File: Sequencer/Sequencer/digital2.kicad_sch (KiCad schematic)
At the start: 4 parts, among them SW5 SW_Rotary12, SW6 SW_Push_DPDT, SW7 SW_Rotary4, U5 4514

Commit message: minor progress on sequencer
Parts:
- added C5 (x3): 1nF, Capacitor_THT:C_Disc_D3.0mm_W1.6mm_P2.50mm, symbol Device:C
- added D11 (x3): 1N914, Diode_THT:D_DO-35_SOD27_P7.62mm_Horizontal, symbol Diode:1N914
- added R12 (x2): 100K, Resistor_THT:R_Axial_DIN0207_L6.3mm_D2.5mm_P7.62mm_Horizontal, symbol Device:R
- added R12 (x2): 1K, Resistor_THT:R_Axial_DIN0207_L6.3mm_D2.5mm_P7.62mm_Horizontal, symbol Device:R
- added R12: 4.7K, Resistor_THT:R_Axial_DIN0207_L6.3mm_D2.5mm_P7.62mm_Horizontal, symbol Device:R
- added R12: 3K, Resistor_THT:R_Axial_DIN0207_L6.3mm_D2.5mm_P7.62mm_Horizontal, symbol Device:R
- added U6: 40106, symbol 4xxx:40106
- SW5: footprint (none) -> Library:rotary_switch_1P12T
- SW7: footprint (none) -> Library:rotary_switch_3P4T
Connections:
- net step_controls10/Step is gone; now on net S10: U5.17 (Q9)
- net step_controls11/Step is gone; now on net S11: U5.20 (Q10)
- net step_controls12/Step is gone; now on net S12: U5.19 (Q11)
- net step_controls13/Step is gone; now on net S13: U5.14 (Q12)
- net step_controls14/Step is gone; now on net S14: U5.13 (Q13)
- net step_controls15/Step is gone; now on net S15: U5.16 (Q14)
- net step_controls16/Step is gone; now on net S16: U5.15 (Q15)
- net step_controls3/Step is gone; now on net S3: U5.10 (Q2)
- net step_controls4/Step is gone; now on net S4: U5.8 (Q3)
- net step_controls5/Step is gone; now on net S5: U5.7 (Q4)
- net step_controls6/Step is gone; now on net S6: U5.6 (Q5)
- net step_controls7/Step is gone; now on net S7: U5.5 (Q6)
- net step_controls8/Step is gone; now on net S8: U5.4 (Q7)
- net step_controls9/Step is gone; now on net S9: U5.18 (Q8)
- net at SW5.13: now also D11.2 (A)
- net STP: now reaches SW7.2
- net CLR: now reaches SW7.3
- net REV: now reaches SW7.4
- net at SW7.5: now also SW6.2 (B)
- net +12V: now reaches U5.1 (EL)
- net +12V: now also U5.24 (Vdd), R12.1
- net GND: now reaches U5.12 (Vss)
- net GND: now also SW6.5 (B), U5.23 (~{EN}), C5.1, C5.1, D11.1 (K), D11.1 (K), R12.1, R12.1
- net QA: now reaches U5.2 (A0)
- net QC: now reaches U5.21 (A2)
- net QD: now reaches U5.22 (A3)
- net QB: now reaches U5.3 (A1)
- net at SW6.1 (A): now also D11.1 (K)
- net RND: now reaches SW6.6 (C)
- new net: R12.2, U6.8
- new net: C5.1, U6.6, U6.9
- new net: R12.2, U6.10
- new net: C5.2, R12.2, U6.11
- new net: D11.2 (A), D11.2 (A), R12.1, U6.5
- new net CBUS: R12.2
- new net GATE: C5.2, R12.1
- new net GB: R12.2, R12.2
- new net TRIG: C5.2, R12.1
- no-connect marks 0 -> 3
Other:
- moved on the sheet: SW6, SW7

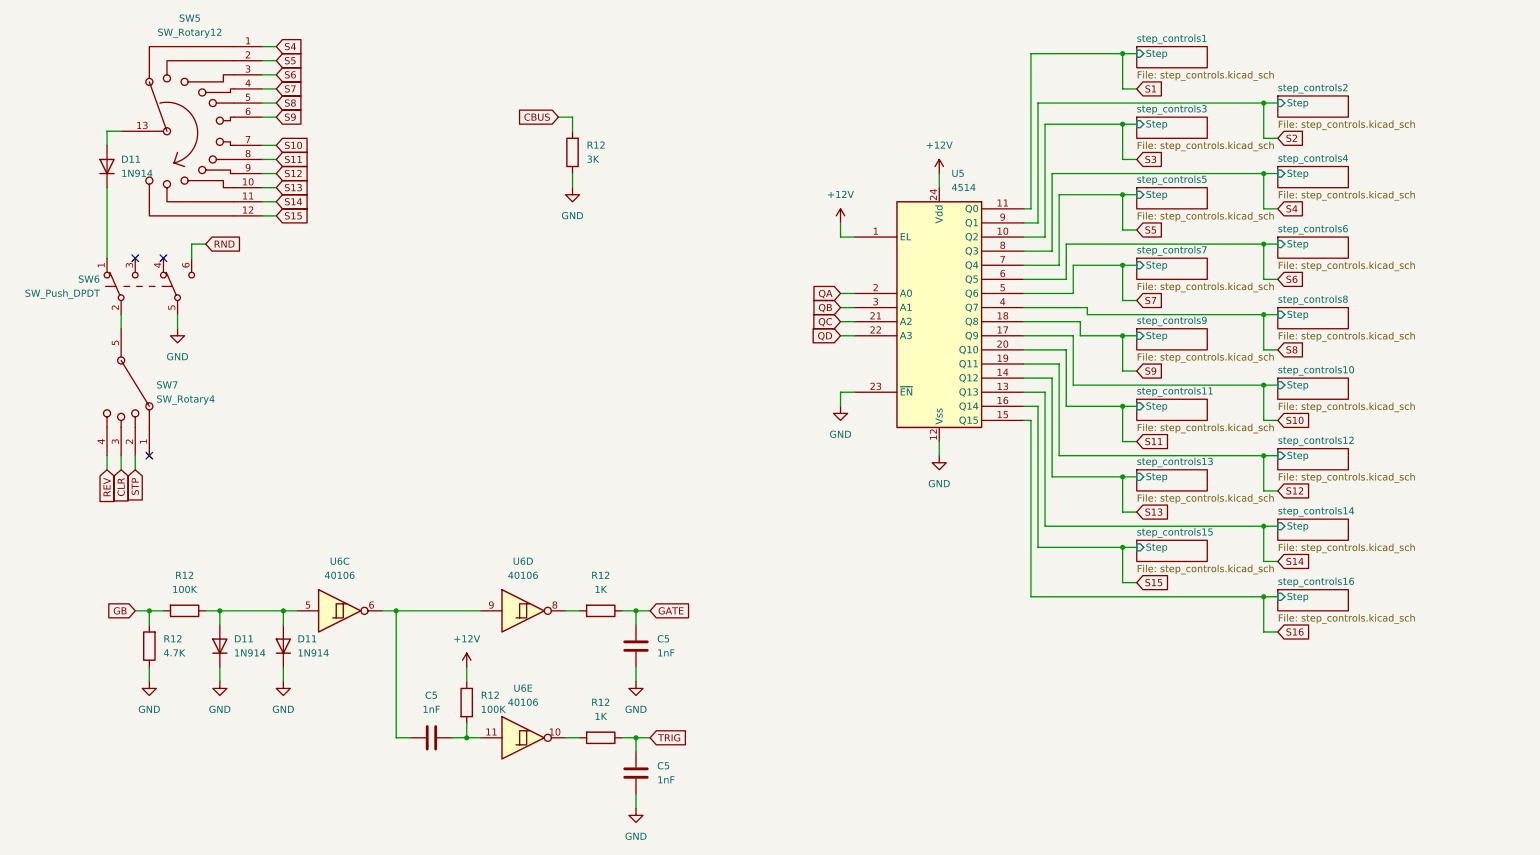
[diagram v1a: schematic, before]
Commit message: Sequencer - schematic mostly complete
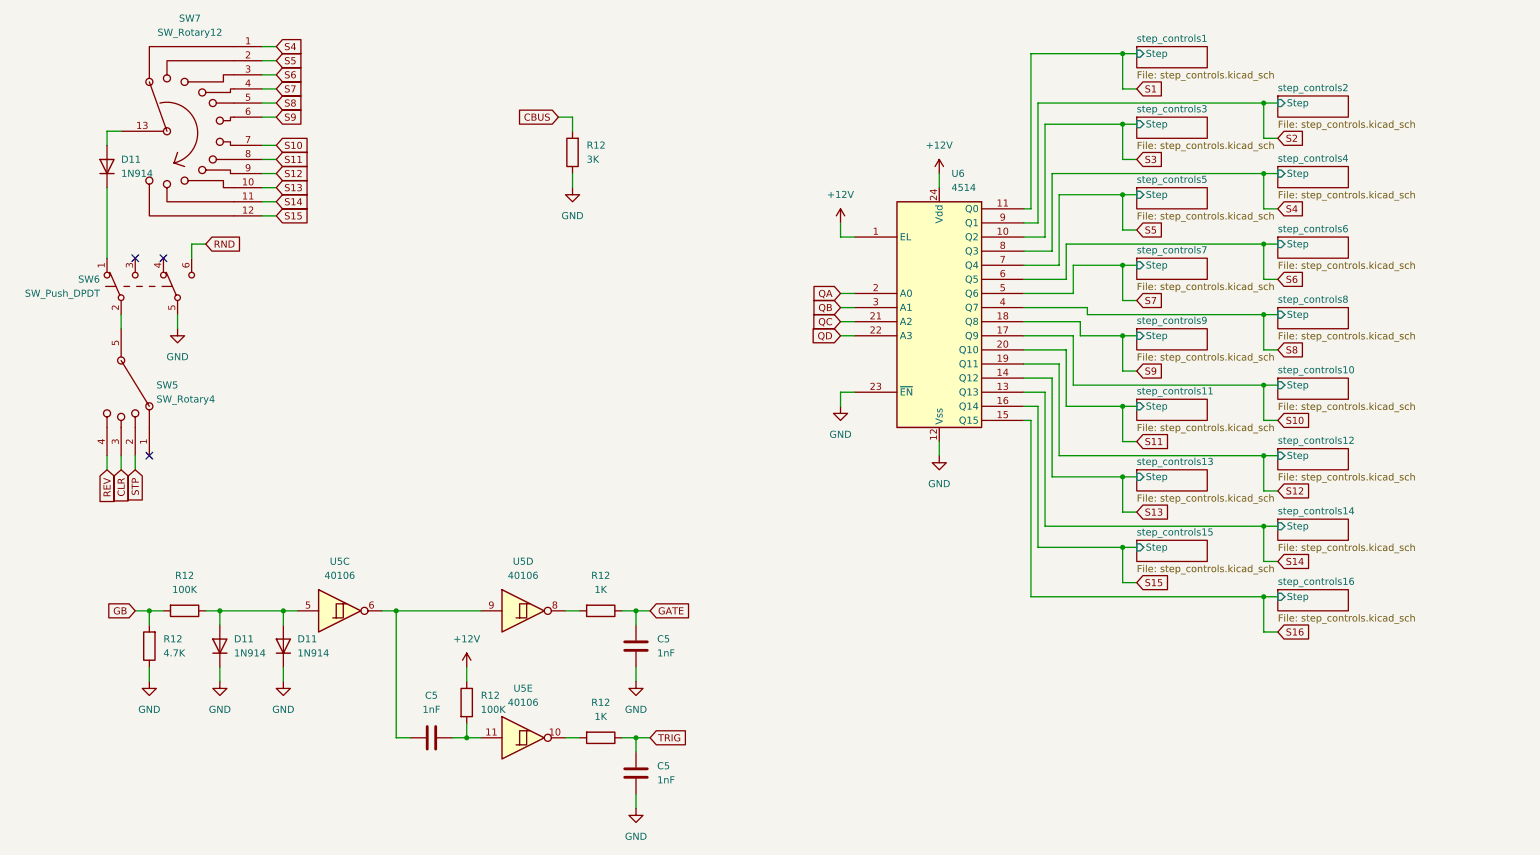
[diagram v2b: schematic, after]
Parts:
- U5: renamed from U6; footprint (none) -> Package_DIP:DIP-14_W7.62mm_Socket_LongPads
- U6: renamed from U5; footprint (none) -> Package_SO:SOIC-24W_7.5x15.4mm_P1.27mm
- renumbered SW7 to SW5, SW5 to SW7

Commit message: Sequencer - minor progress on routing
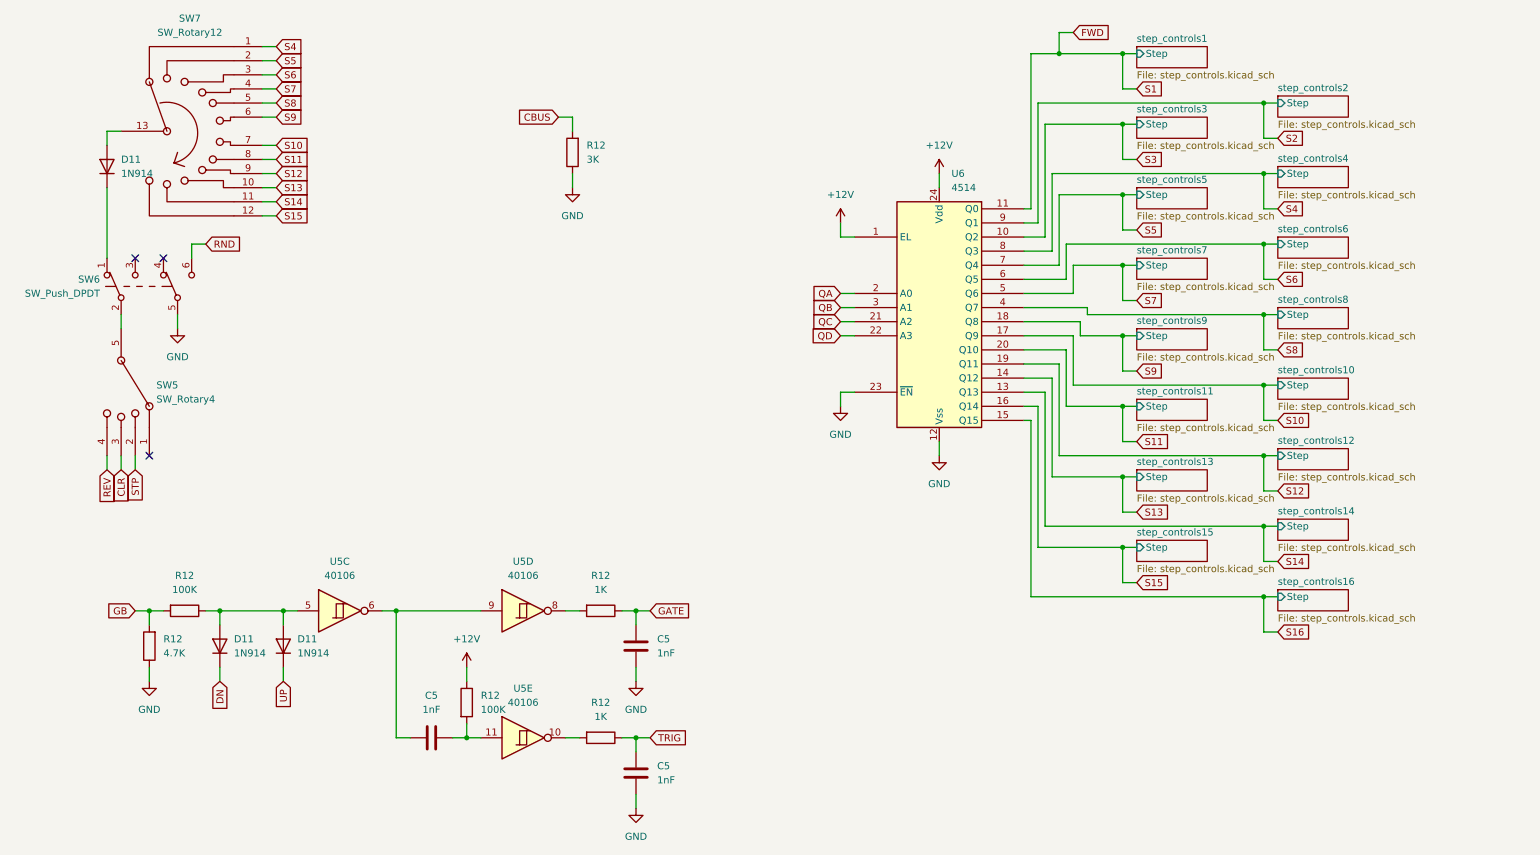
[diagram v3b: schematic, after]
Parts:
- C5: footprint Capacitor_THT:C_Disc_D3.0mm_W1.6mm_P2.50mm -> Capacitor_THT:C_Disc_D5.0mm_W2.5mm_P2.50mm
- R12: footprint Resistor_THT:R_Axial_DIN0207_L6.3mm_D2.5mm_P7.62mm_Horizontal -> Library:R_Axial_DIN0207_L6.3mm_D2.5mm_P7.62mm_Horizontal
- U6: footprint Package_SO:SOIC-24W_7.5x15.4mm_P1.27mm -> Package_DIP:DIP-24_W15.24mm_Socket_LongPads
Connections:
- net GND: no longer D11.1 (K), D11.1 (K)
- net S1 renamed FWD
- new net DN: D11.1 (K)
- new net UP: D11.1 (K)
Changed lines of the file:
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@@
   (junction (at 200.66 90.17) (diameter 0) (color 0 0 0 0)
+  )
+  (junction (at 189.23 26.67) (diameter 0) (color 0 0 0 0)
   )
   (junction (at 49.53 127) (diameter 0) (color 0 0 0 0)
@@
     (stroke (width 0) (type default))
   )
-  (wire (pts (xy 184.15 26.67) (xy 200.66 26.67))
+  (wire (pts (xy 184.15 26.67) (xy 189.23 26.67))
     (stroke (width 0) (type default))
   )
@@
     (stroke (width 0) (type default))
   )
+  (wire (pts (xy 191.77 22.86) (xy 189.23 22.86))
+    (stroke (width 0) (type default))
+  )
   (wire (pts (xy 187.96 62.23) (xy 187.96 48.26))
     (stroke (width 0) (type default))
@@
     (stroke (width 0) (type default))
   )
+  (wire (pts (xy 189.23 26.67) (xy 200.66 26.67))
+    (stroke (width 0) (type default))
+  )
   (wire (pts (xy 110.49 127) (xy 113.03 127))
     (stroke (width 0) (type default))
@@
   )
   (wire (pts (xy 226.06 48.26) (xy 228.6 48.26))
+    (stroke (width 0) (type default))
+  )
+  (wire (pts (xy 189.23 22.86) (xy 189.23 26.67))
     (stroke (width 0) (type default))
   )
@@
     )
   )
+  (global_label "DN" (shape input) (at 38.1 139.7 270) (fields_autoplaced)
+    (effects (font (size 1.27 1.27)) (justify right))
+    (property "Intersheetrefs" "${INTERSHEET_REFS}" (at 38.1 145.2857 90)
+      (effects (font (size 1.27 1.27)) (justify right) hide)
+    )
+  )
   (global_label "S10" (shape input) (at 228.6 92.71 0) (fields_autoplaced)
     (effects (font (size 1.27 1.27)) (justify left))
@@
     )
   )
+  (global_label "UP" (shape input) (at 49.53 139.7 270) (fields_autoplaced)
+    (effects (font (size 1.27 1.27)) (justify right))
+    (property "Intersheetrefs" "${INTERSHEET_REFS}" (at 49.53 145.2857 90)
+      (effects (font (size 1.27 1.27)) (justify right) hide)
+    )
+  )
   (global_label "REV" (shape input) (at 17.78 101.6 270) (fields_autoplaced)
     (effects (font (size 1.27 1.27)) (justify right))
@@
     )
   )
+  (global_label "FWD" (shape input) (at 191.77 22.86 0) (fields_autoplaced)
+    (effects (font (size 1.27 1.27)) (justify left))
+    (property "Intersheetrefs" "${INTERSHEET_REFS}" (at 198.5652 22.86 0)
+      (effects (font (size 1.27 1.27)) (justify left) hide)
+    )
+  )
   (global_label "S11" (shape input) (at 203.2 96.52 0) (fields_autoplaced)
     (effects (font (size 1.27 1.27)) (justify left))
@@
     (property "Intersheetrefs" "${INTERSHEET_REFS}" (at 208.6042 45.72 0)
       (effects (font (size 1.27 1.27)) (justify left) hide)
-    )
-  )
-  (symbol (lib_id "power:GND") (at 49.53 139.7 0) (unit 1)
-    (in_bom yes) (on_board yes) (dnp no) (fields_autoplaced)
-    (property "Reference" "#PWR033" (at 49.53 146.05 0)
-      (effects (font (size 1.27 1.27)) hide)
-    )
-    (property "Value" "GND" (at 49.53 144.78 0)
-      (effects (font (size 1.27 1.27)))
-    )
-    (property "Footprint" "" (at 49.53 139.7 0)
-      (effects (font (size 1.27 1.27)) hide)
-    )
-    (property "Datasheet" "" (at 49.53 139.7 0)
-      (effects (font (size 1.27 1.27)) hide)
-    )
-    (pin "1")
-    (instances
-      (project "Sequencer"
-        (path "/8a8c4421-b74b-4a68-822a-0aad66407659/46b6ac52-1a8a-4365-bf12-f4a4e535ecf0"
-          (reference "#PWR033") (unit 1)
-        )
-      )
     )
   )
@@
       (effects (font (size 1.27 1.27)) (justify right))
     )
-    (property "Footprint" "Capacitor_THT:C_Disc_D3.0mm_W1.6mm_P2.50mm" (at 112.0648 129.54 0)
+    (property "Footprint" "Capacitor_THT:C_Disc_D5.0mm_W2.5mm_P2.50mm" (at 112.0648 129.54 0)
       (effects (font (size 1.27 1.27)) hide)
     )
@@
       (effects (font (size 1.27 1.27)))
     )
-    (property "Footprint" "Resistor_THT:R_Axial_DIN0207_L6.3mm_D2.5mm_P7.62mm_Horizontal" (at 31.75 125.222 90)
+    (property "Footprint" "Library:R_Axial_DIN0207_L6.3mm_D2.5mm_P7.62mm_Horizontal" (at 31.75 125.222 90)
       (effects (font (size 1.27 1.27)) hide)
     )
@@
       (effects (font (size 1.27 1.27)) (justify right))
     )
-    (property "Footprint" "Capacitor_THT:C_Disc_D3.0mm_W1.6mm_P2.50mm" (at 112.0648 152.4 0)
+    (property "Footprint" "Capacitor_THT:C_Disc_D5.0mm_W2.5mm_P2.50mm" (at 112.0648 152.4 0)
       (effects (font (size 1.27 1.27)) hide)
     )
@@
       (effects (font (size 1.27 1.27)))
     )
-    (property "Footprint" "Resistor_THT:R_Axial_DIN0207_L6.3mm_D2.5mm_P7.62mm_Horizontal" (at 106.68 148.082 90)
+    (property "Footprint" "Library:R_Axial_DIN0207_L6.3mm_D2.5mm_P7.62mm_Horizontal" (at 106.68 148.082 90)
       (effects (font (size 1.27 1.27)) hide)
     )
@@
       (effects (font (size 1.27 1.27)))
     )
-    (property "Footprint" "Resistor_THT:R_Axial_DIN0207_L6.3mm_D2.5mm_P7.62mm_Horizontal" (at 106.68 125.222 90)
+    (property "Footprint" "Library:R_Axial_DIN0207_L6.3mm_D2.5mm_P7.62mm_Horizontal" (at 106.68 125.222 90)
       (effects (font (size 1.27 1.27)) hide)
     )
@@
     )
   )
-  (symbol (lib_id "power:GND") (at 38.1 139.7 0) (unit 1)
-    (in_bom yes) (on_board yes) (dnp no) (fields_autoplaced)
-    (property "Reference" "#PWR032" (at 38.1 146.05 0)
-      (effects (font (size 1.27 1.27)) hide)
-    )
-    (property "Value" "GND" (at 38.1 144.78 0)
-      (effects (font (size 1.27 1.27)))
-    )
-    (property "Footprint" "" (at 38.1 139.7 0)
-      (effects (font (size 1.27 1.27)) hide)
-    )
-    (property "Datasheet" "" (at 38.1 139.7 0)
-      (effects (font (size 1.27 1.27)) hide)
-    )
-    (pin "1")
-    (instances
-      (project "Sequencer"
-        (path "/8a8c4421-b74b-4a68-822a-0aad66407659/46b6ac52-1a8a-4365-bf12-f4a4e535ecf0"
-          (reference "#PWR032") (unit 1)
-        )
-      )
-    )
-  )
   (symbol (lib_id "Device:R") (at 25.4 133.35 180) (unit 1)
     (in_bom yes) (on_board yes) (dnp no) (fields_autoplaced)
@@
       (effects (font (size 1.27 1.27)) (justify right))
     )
-    (property "Footprint" "Resistor_THT:R_Axial_DIN0207_L6.3mm_D2.5mm_P7.62mm_Horizontal" (at 27.178 133.35 90)
+    (property "Footprint" "Library:R_Axial_DIN0207_L6.3mm_D2.5mm_P7.62mm_Horizontal" (at 27.178 133.35 90)
       (effects (font (size 1.27 1.27)) hide)
     )
@@
       (effects (font (size 1.27 1.27)) (justify left))
     )
-    (property "Footprint" "Package_SO:SOIC-24W_7.5x15.4mm_P1.27mm" (at 167.64 73.66 0)
+    (property "Footprint" "Package_DIP:DIP-24_W15.24mm_Socket_LongPads" (at 167.64 73.66 0)
       (effects (font (size 1.27 1.27)) hide)
     )
@@
       (effects (font (size 1.27 1.27)) (justify left))
     )
-    (property "Footprint" "Resistor_THT:R_Axial_DIN0207_L6.3mm_D2.5mm_P7.62mm_Horizontal" (at 80.772 143.51 90)
+    (property "Footprint" "Library:R_Axial_DIN0207_L6.3mm_D2.5mm_P7.62mm_Horizontal" (at 80.772 143.51 90)
       (effects (font (size 1.27 1.27)) hide)
     )
@@
       (effects (font (size 1.27 1.27)))
     )
-    (property "Footprint" "Capacitor_THT:C_Disc_D3.0mm_W1.6mm_P2.50mm" (at 80.01 148.8948 0)
+    (property "Footprint" "Capacitor_THT:C_Disc_D5.0mm_W2.5mm_P2.50mm" (at 80.01 148.8948 0)
       (effects (font (size 1.27 1.27)) hide)
     )
@@
       (effects (font (size 1.27 1.27)) (justify right))
     )
-    (property "Footprint" "Resistor_THT:R_Axial_DIN0207_L6.3mm_D2.5mm_P7.62mm_Horizontal" (at 103.378 44.45 90)
-      (effects (font (size 1.27 1.27)) hide)
-    )
+    (property "Footprint" "Library:R_Axial_DIN0207_L6.3mm_D2.5mm_P7.62mm_Horizontal" (at 103.378 44.45 90)
+      (effects (font (size 1.27 1.27)) hide)
+    )
